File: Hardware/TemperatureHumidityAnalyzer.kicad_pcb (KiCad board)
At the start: 2 copper layers, 29 parts, among them J1 Power, J2 SSD1306 Display, J3 SWD, SW1 SW_Push, SW2 SW_Nidec_CAS-120A1, U1 AMS1117-3.3, U2 HDC2010YPAR, U3 STM32L432KCU6, Y1 8MHz Crystal

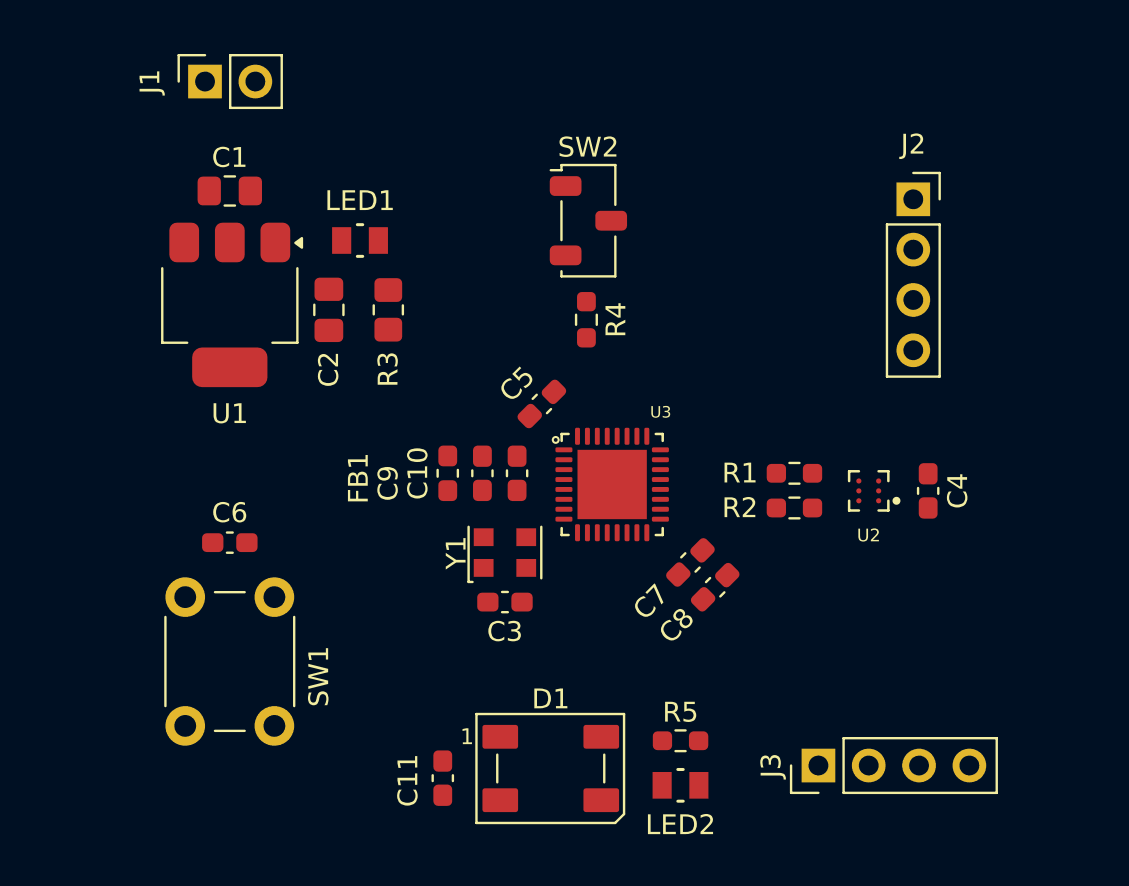
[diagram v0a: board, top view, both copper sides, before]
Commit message: Add mounting holes
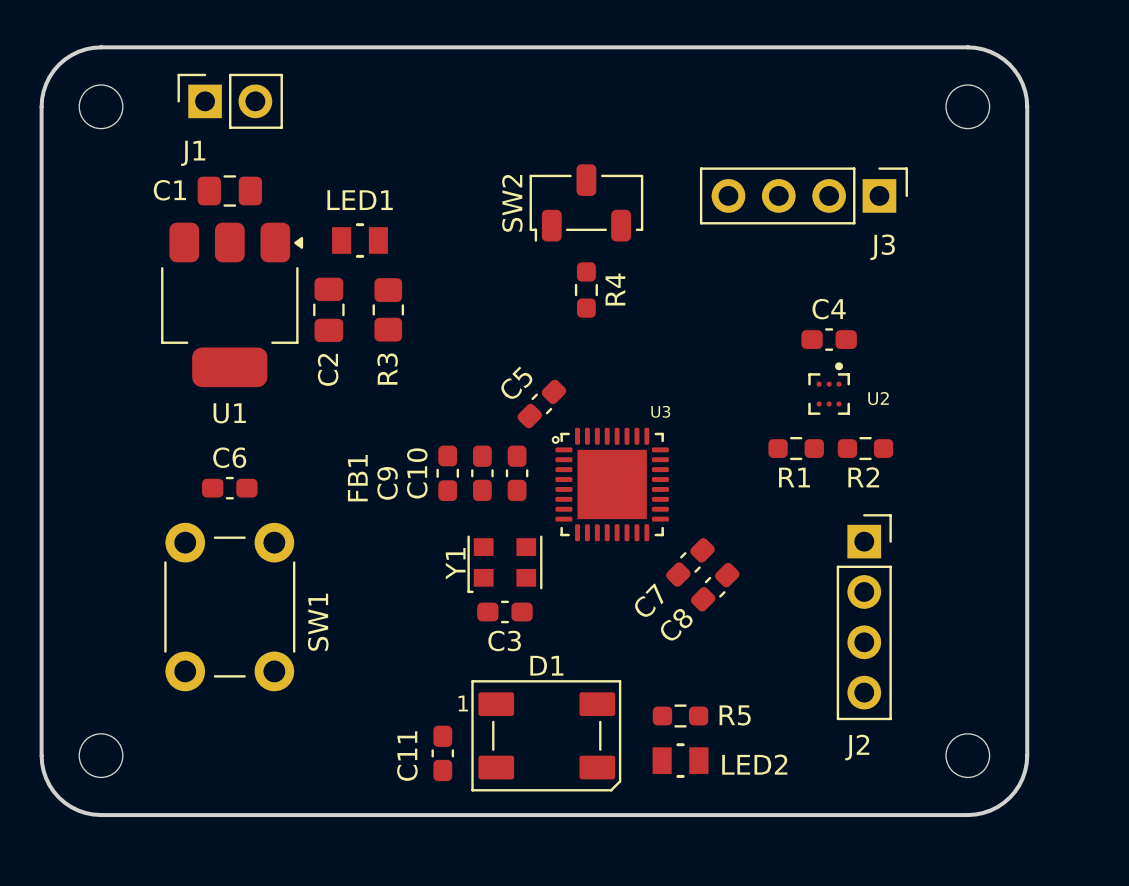
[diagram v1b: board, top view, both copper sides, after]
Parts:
- added H1: MountingHole, MountingHole:MountingHole_2.2mm_M2, F.Cu at (71.0, 106.8)
- added H2: MountingHole, MountingHole:MountingHole_2.2mm_M2, F.Cu at (114.8, 106.8)
- added H3: MountingHole, MountingHole:MountingHole_2.2mm_M2, F.Cu at (114.8, 139.5)
- added H4: MountingHole, MountingHole:MountingHole_2.2mm_M2, F.Cu at (71.0, 139.5)
- moved J3 28.9 mm to (110.3, 111.2), turned to -90 degrees
- moved J2 17.5 mm to (109.5, 128.7)
- moved C4 9.13 mm to (107.8, 118.5), turned to 180 degrees
- moved U2 5.28 mm to (107.8, 121.2), turned to -90 degrees
- moved R2 4.68 mm to (109.6, 124.0), turned to 0 degrees
- moved C6 2.75 mm to (77.5, 126.0)
- moved SW1 2.75 mm to (79.8, 128.8)
- moved D1 1.66 mm to (93.5, 138.5)
- moved R4 1.50 mm to (95.5, 116.0)
- moved R1 1.25 mm to (106.1, 124.0)
- moved C11 1.25 mm to (88.2, 139.4)
- moved LED2 1.25 mm to (100.2, 139.8)
- moved R5 1.25 mm to (100.2, 137.5)
- moved J1 1.00 mm to (76.2, 106.5)
- moved SW2 0.91 mm to (95.5, 111.6), turned to 90 degrees
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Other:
- board outline added: 49.8 x 38.8 mm

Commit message: Finish pcb layout
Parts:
- moved D1 10.3 mm to (83.2, 137.5), turned to -90 degrees
- moved C11 8.84 mm to (83.4, 132.0), turned to 180 degrees
- moved J2 8.44 mm to (113.5, 121.2)
- moved R2 7.00 mm to (102.8, 125.5)
- moved R1 4.49 mm to (102.8, 127.0), turned to 0 degrees
- moved R4 4.17 mm to (93.5, 112.3)
- moved SW2 4.17 mm to (93.5, 107.9)
- moved J3 3.95 mm to (109.0, 107.5)
- moved SW1 3.25 mm to (76.8, 127.5)
- moved C6 3.16 mm to (74.5, 125.0)
- moved R5 1.51 mm to (98.8, 138.0)
- moved LED2 1.45 mm to (98.8, 140.0)
- moved C10 0.50 mm to (91.5, 125.2)
- moved C9 0.50 mm to (89.8, 125.2)
- moved FB1 0.50 mm to (88.0, 125.2)

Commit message: Route pcb
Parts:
- moved R4 2.14 mm to (95.6, 112.2)
- moved C1 2.14 mm to (79.6, 110.9)
- moved C10 2.14 mm to (93.6, 125.1)
- moved C11 2.14 mm to (85.5, 131.9)
- moved C2 2.14 mm to (84.6, 116.9)
- moved C3 2.14 mm to (93.5, 132.1)
- moved C4 2.14 mm to (109.9, 118.4)
- moved C5 2.14 mm to (95.4, 121.6)
- moved C6 2.14 mm to (76.6, 124.9)
- moved C7 2.14 mm to (102.9, 129.6)
- moved C8 2.14 mm to (104.1, 130.9)
- moved C9 2.14 mm to (91.9, 125.1)
- moved D1 2.14 mm to (85.4, 137.4)
- moved FB1 2.14 mm to (90.1, 125.1)
- moved H1 2.14 mm to (73.1, 106.6)
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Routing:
- net +3.3V: track 0.00 -> 143.5 mm, vias 0 -> 2
- net GND: track 0.00 -> 52.4 mm, vias 0 -> 34
- net SDA_Display: track 0.00 -> 35.2 mm, vias 0 -> 2
- net /NRST: track 0.00 -> 29.2 mm, vias 0 -> 2
- net SCL_Display: track 0.00 -> 26.3 mm, vias 0 -> 2
- net CUSTOM_LED: track 0.00 -> 22.1 mm, vias 0 -> 2
- net SWDIO: track 0.00 -> 20.6 mm
- net SWCLK: track 0.00 -> 18.5 mm
- net SCL_Temp: track 0.00 -> 16.2 mm, vias 0 -> 2
- net SDA_Temp: track 0.00 -> 13.0 mm, vias 0 -> 2
- net /BOOT0: track 0.00 -> 11.0 mm
- net INT_Temp: track 0.00 -> 10.4 mm, vias 0 -> 2
- net BLINK_LED: track 0.00 -> 9.81 mm
- net +3.3VA: track 0.00 -> 6.39 mm
- net Net-(SW2-B): track 0.00 -> 4.64 mm
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- added copper zone on F.Cu, net +3.3V
- added copper zone on F.Cu, net +9V
- added copper zone on B.Cu, net GND
- added copper zone on F.Cu, net GND

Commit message: Generate manufacturing files
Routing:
- net +3.3V: track 143.5 -> 165.1 mm
- net GND: track 52.4 -> 61.2 mm, vias 34 -> 28
- net INT_Temp: track 10.4 -> 9.60 mm, vias 2 -> 0
- net CUSTOM_LED: vias 2 -> 0
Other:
- board text added: "9V"
- board text added: "BOOT"
- board text added: "Dash Campbell 8/26 v0.1"
- board text added: "GND"
- board text added: "NRST"
- board text added: "SWD"
